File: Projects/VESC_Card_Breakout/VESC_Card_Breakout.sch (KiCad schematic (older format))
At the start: 5 parts, among them P1 USB_OTG, P2 CONN_01X02, P3 CONN_01X04

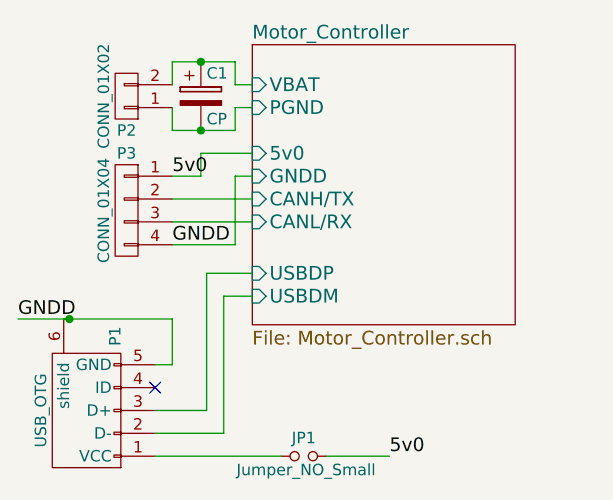
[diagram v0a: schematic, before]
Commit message: finished reconnecting stuff on VESC
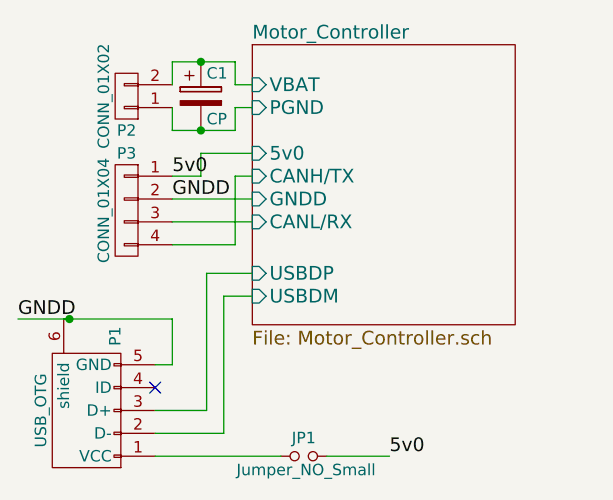
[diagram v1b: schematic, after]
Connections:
- net GNDD: now also P3.2 (P2); no longer P3.4 (P4)
- net Motor_Controller/CANH/TX: now also P3.4 (P4); no longer P3.2 (P2)
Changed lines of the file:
@@
 EESchema Schematic File Version 2
+LIBS:VESC_Card_Breakout-rescue
 LIBS:power
 LIBS:device
@@
 F2 "VBAT" I L 5200 3350 60
 F3 "PGND" I L 5200 3450 60
-F4 "CANH/TX" I L 5200 3850 60
+F4 "CANH/TX" I L 5200 3750 60
 F5 "CANL/RX" I L 5200 3950 60
 F6 "USBDP" I L 5200 4175 60
 F7 "USBDM" I L 5200 4275 60
-F8 "GNDD" I L 5200 3750 60
+F8 "GNDD" I L 5200 3850 60
 F9 "5v0" I L 5200 3650 60
 $EndSheet
@@
 Wire Wire Line
 	5125 4050 4850 4050
-Text Label 4850 4050 0    60   ~ 0
+Text Label 4850 3850 0    60   ~ 0
 GNDD
 Text Label 4850 3750 0    60   ~ 0
